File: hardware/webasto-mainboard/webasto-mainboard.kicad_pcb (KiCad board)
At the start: 4 copper layers, 86.8 x 76 mm, 100 parts, among them J1 Console FTDI, J2 DEBUG, J3 2-pole connector, Q1 DMG2301L, Q10 DMG2301L, Q11 SSM3J374R, Q12 2N7002, Q13 SUD50P04-08, Q14 SUD50P04-08, Q15 SUD50P04-08, Q16 SUD50P04-08, Q17 SUD50P04-08, Q18 2N7002, Q19 2N7002, Q2 2N7002, Q3 2N7002, Q4 2N7002, Q5 2N7002, Q6 SUD50P04-08, Q7 SUD50P04-08, Q8 SUD50P04-08, Q9 SUD50P04-08, U1 CY15E004J, U2 Pico, U3 LM4040DIM3-3.0, U4 MC33660BEFR2, U5 BD9G341EFJ, U6 LM7805_TO220, U7 INA219BxDCN

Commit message: Moved emerg. shutdown offboard
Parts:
- removed the D7 at (120.5, 103.9)
- removed the R16 at (136.1, 106.6)
- removed the R19 at (120.5, 103.9)
- J3: value 2-pole connector -> I2C; footprint Connector_PinHeader_2.54mm:PinHeader_1x02_P2.54mm_Horizontal -> Connector_PinHeader_2.54mm:PinHeader_1x04_P2.54mm_Vertical
- moved J3 8.16 mm to (108.5, 99.5), turned to 90 degrees
- renumbered D11 to D10, D12 to D11, D13 to D12, D8 to D7, D9 to D8, D10 to D9, R17 to R16, R18 to R17, R20 to R18, R21 to R19, R22 to R20, R23 to R21, R24 to R22, R25 to R23, R26 to R24, R27 to R25, R28 to R26, R29 to R27, R30 to R28, R31 to R29, R32 to R30, R33 to R31, R34 to R32, R35 to R33, R36 to R34
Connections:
- J3 pad 1: EmergencyStop -> SDA
- J3 pad 2: GND -> SCL
- U2 pad 21: ~{EmergencyStop3V} -> unconnected-(U2-Pad21)
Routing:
- net SDA: track 84.7 -> 140.1 mm, vias 2 -> 3
- net SCL: track 81.9 -> 130.7 mm, vias 3 -> 4
- net ~{EmergencyStop3V}: track 19.7 -> 0.00 mm, vias 1 -> 0
- net +3V3: track 50.6 -> 62.3 mm
- net ~{EmergencyStop}: track 6.21 -> 0.00 mm, vias 1 -> 0
- net Net-(Q2-Pad1): track 53.5 -> 50.3 mm
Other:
- board text added: "SDA SCL VCC GND"
- board text added: "v2.0 (c) 2023 Gavin Hurlbut"
- board text removed: "v1.0 (c) 2023 Gavin Hurlbut"

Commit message: Got rid of TINY diode (0402!?!?), remove USE_USB, put in PicoW
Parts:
- removed the J2 at (131.0, 98.2)
- removed JP1: SolderJumper_2_Open, Jumper:SolderJumper-2_P1.3mm_Open_TrianglePad1.0x1.5mm
- removed the R1 at (139.0, 104.6)
- C12: footprint Capacitor_SMD:C_0603_1608Metric_Pad1.08x0.95mm_HandSolder -> Capacitor_SMD:C_0805_2012Metric_Pad1.18x1.45mm_HandSolder
- D10: value ACDBQC0130L-HF -> BYS10-35; footprint Diode_SMD:D_SOD-923 -> Diode_SMD:D_SMA_Handsoldering; moved to F.Cu
- D7: value ACDBQC0130L-HF -> BYS10-35; footprint Diode_SMD:D_SOD-923 -> Diode_SMD:D_SMA_Handsoldering
- U2: value Pico -> PicoW; footprint MCU_RaspberryPi_and_Boards:RPi_Pico_SMD_TH -> RPi_Pico:RPi_PicoW_SMD_TH
- moved D10 5.44 mm to (104.5, 118.3), turned to 135 degrees
- moved D7 3.65 mm to (132.0, 71.4)
- moved D9 1.63 mm to (130.3, 67.8)
- moved C6 1.56 mm to (130.3, 64.6)
- renumbered J3 to J2, R2 to R1, R11 to R10, R12 to R11, R13 to R12, R14 to R13, R15 to R14, R16 to R15, R17 to R16, R18 to R17, R19 to R18, R20 to R19, R3 to R2, R21 to R20, R22 to R21, R23 to R22, R24 to R23, R25 to R24, R26 to R25, R27 to R26, R28 to R27, R29 to R28, R30 to R29, R4 to R3, R31 to R30, R32 to R31, R33 to R32, R34 to R33, R5 to R4, R6 to R5, R7 to R6, R8 to R7, R9 to R8, R10 to R9
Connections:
- U2 pad 22: UseUSB -> unconnected-(U2-Pad22)
- U2 pad 41: Net-(J2-Pad1) -> unconnected-(U2-Pad41)
- U2 pad 43: Net-(J2-Pad3) -> unconnected-(U2-Pad43)
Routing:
- net Net-(C7-Pad2): track 14.3 -> 21.0 mm
- net UseUSB: track 6.37 -> 0.00 mm
- net Net-(J2-Pad3): track 5.36 -> 0.00 mm
- net Net-(J2-Pad1): track 5.36 -> 0.00 mm
- net GND: track 63.1 -> 58.2 mm, vias 15 -> 16
- net Net-(D1-Pad2): track 38.8 -> 43.6 mm
- net +3V3: track 62.3 -> 59.1 mm, vias 10 -> 9
- net Net-(D7-Pad1): track 2.89 -> 4.59 mm
- net +12V: track 28.9 -> 27.8 mm, vias 13 -> 12

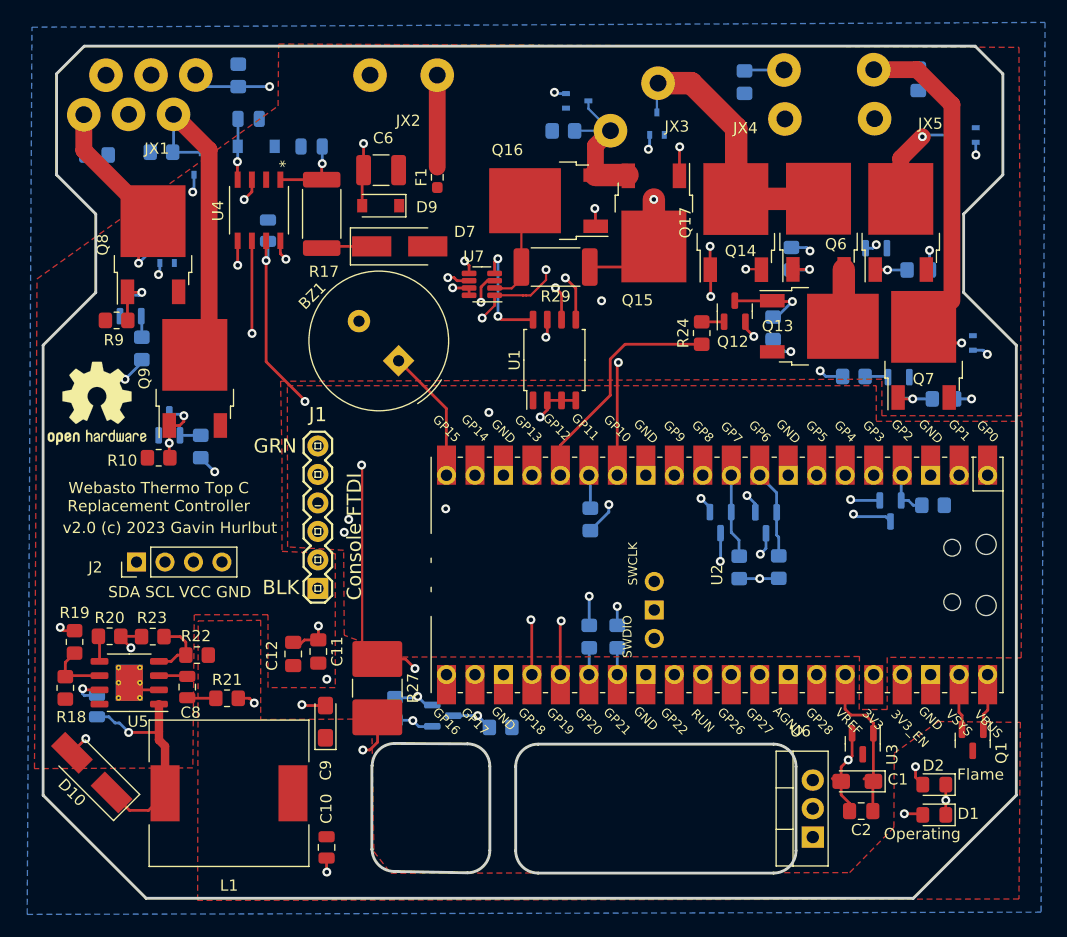
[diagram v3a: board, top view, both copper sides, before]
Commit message: Move VSYS to ADC2 to avoid the stupid WiFi setup
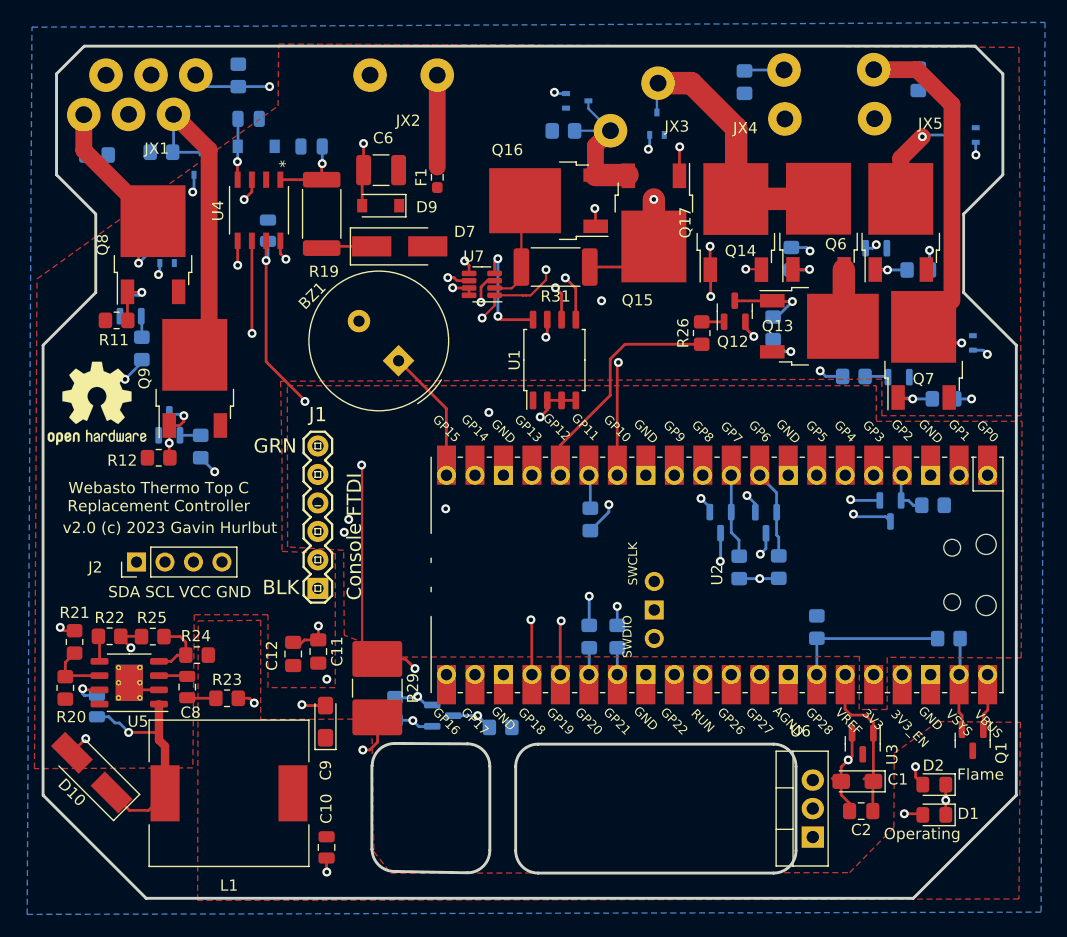
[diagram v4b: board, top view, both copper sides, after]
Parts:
- added R1: 200k, Resistor_SMD:R_0805_2012Metric_Pad1.20x1.40mm_HandSolder, B.Cu at (181.0, 106.4)
- added R2: 100k, Resistor_SMD:R_0805_2012Metric_Pad1.20x1.40mm_HandSolder, B.Cu at (169.2, 105.3)
- renumbered R8 to R10, R9 to R11, R10 to R12, R11 to R13, R12 to R14, R13 to R15, R14 to R16, R15 to R17, R16 to R18, R17 to R19, R18 to R20, R19 to R21, R20 to R22, R21 to R23, R22 to R24, R23 to R25, R24 to R26, R25 to R27, R26 to R28, R27 to R29, R1 to R3, R28 to R30, R29 to R31, R30 to R32, R31 to R33, R32 to R34, R33 to R35, R2 to R4, R3 to R5, R4 to R6, R5 to R7, R6 to R8, R7 to R9
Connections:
- net /ADC_VREF renamed ADC_VREF
- net /VSYS renamed VSYS
- U2 pad 34: unconnected-(U2-Pad34) -> VSYS_MON
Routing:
- net VSYS_MON: track 0.00 -> 14.0 mm
- net VSYS: track 5.00 -> 8.25 mm

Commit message: Move the LED to the mainboard
- due to how the driver doesn't share the SPI bus well, you currently can
  either use the TCP stack or the GPIOs.  Mixing will cause weird crashes.
- so I'm adding the LED onto the mainboard directly.
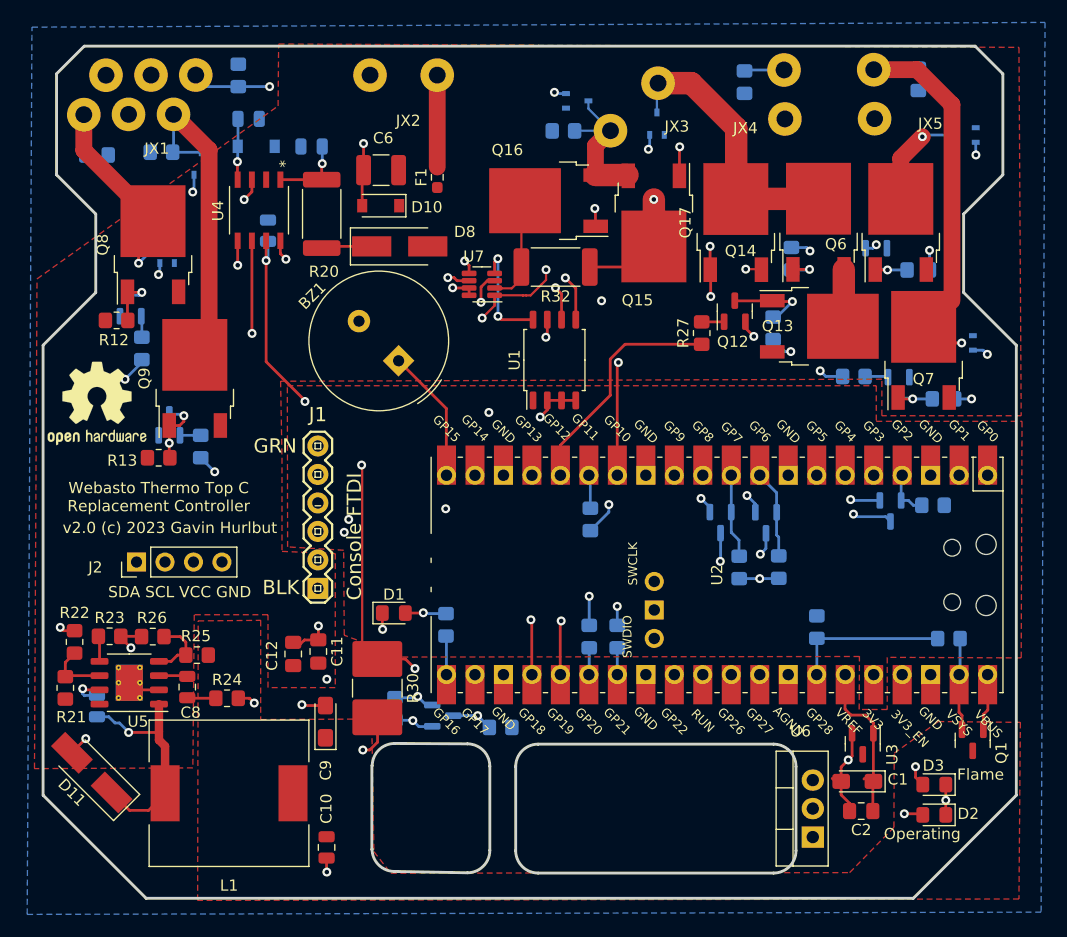
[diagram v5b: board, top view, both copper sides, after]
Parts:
- added D1: LED, LED_SMD:LED_0805_2012Metric_Pad1.15x1.40mm_HandSolder, F.Cu at (131.5, 104.1)
- added R3: 330R, Resistor_SMD:R_0805_2012Metric_Pad1.20x1.40mm_HandSolder, B.Cu at (136.1, 105.2)
- renumbered D9 to D10, D10 to D11, D11 to D12, D12 to D13, D1 to D2, D2 to D3, D3 to D4, D4 to D5, D5 to D6, D6 to D7, D7 to D8, D8 to D9, R9 to R10, R10 to R11, R11 to R12, R12 to R13, R13 to R14, R14 to R15, R15 to R16, R16 to R17, R17 to R18, R18 to R19, R19 to R20, R20 to R21, R21 to R22, R22 to R23, R23 to R24, R24 to R25, R25 to R26, R26 to R27, R27 to R28, R28 to R29, R29 to R30, R30 to R31, R31 to R32, R32 to R33, R33 to R34, R34 to R35, R35 to R36, R3 to R4, R4 to R5, R5 to R6, R6 to R7, R7 to R8, R8 to R9
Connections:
- U2 pad 21: unconnected-(U2-Pad21) -> Net-(U2-Pad21)
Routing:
- net Net-(D1-Pad2): track 0.00 -> 3.67 mm, vias 0 -> 1
- net Net-(U2-Pad21): track 0.00 -> 3.54 mm
- net GND: track 58.2 -> 59.6 mm, vias 16 -> 17

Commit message: Move start/run to sensor board, add CANBUS
- WiFi is not being very helpful, and I'm concerned it won't work well once
  installed in the bus...  CANBus wiring is easy.
- Removed both Start/Run and the Vehicle Fan Relay from X1 to make space for
  canbus
- moved LEDs onto an I2C gpio extender.
- will need to still plumb in CAN_EN support
- will also need to yank out the WiFi stuff that won't stay stable anyways
  and reroute the CBOR out the CANBus instead of WiFi
- Vehicle Fan control will need to move to a LINBus fan controller board
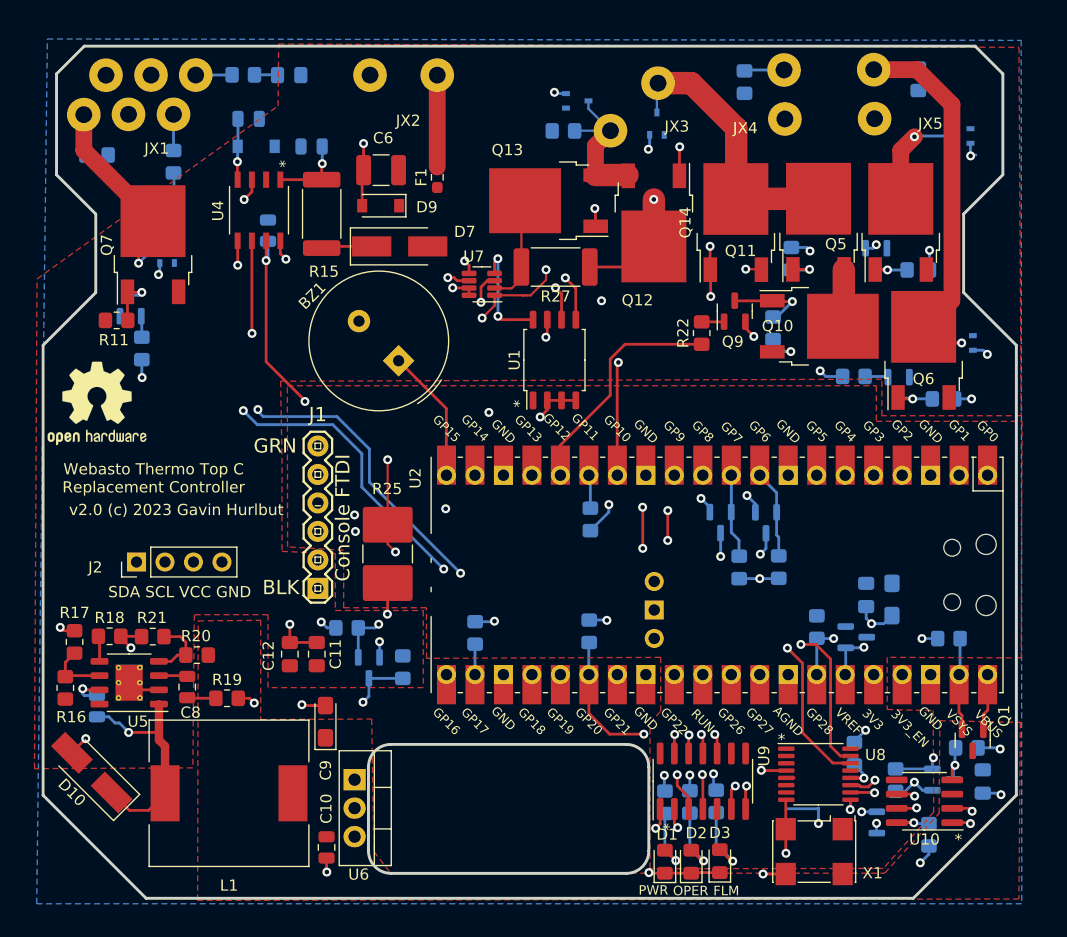
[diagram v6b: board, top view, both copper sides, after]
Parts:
- removed the D6 at (114.3, 64.0)
- removed the Q10 at (175.8, 95.0)
- removed the Q5 at (111.5, 87.3)
- removed the Q9 at (113.7, 83.2)
- removed the R13 at (110.5, 90.2)
- removed the R17 at (110.8, 63.0)
- removed the R18 at (117.6, 56.1)
- removed the R19 at (179.6, 94.5)
- removed the R9 at (114.2, 89.2)
- added C13: 1uF 6V3, Capacitor_SMD:C_0805_2012Metric_Pad1.18x1.45mm_HandSolder, B.Cu at (184.0, 119.1)
- added C14: 560pF, Capacitor_SMD:C_0805_2012Metric_Pad1.18x1.45mm_HandSolder, B.Cu at (122.1, 56.1)
- added C15: 560pF, Capacitor_SMD:C_0805_2012Metric_Pad1.18x1.45mm_HandSolder, B.Cu at (111.9, 67.9)
- added Q17: 2N7002, Package_TO_SOT_SMD:SOT-23, B.Cu at (180.4, 119.0)
- added Q18: 2N7002, Package_TO_SOT_SMD:SOT-23, B.Cu at (175.5, 122.8)
- added R32: 10k, Resistor_SMD:R_0805_2012Metric_Pad1.20x1.40mm_HandSolder, B.Cu at (138.7, 105.9)
- added R33: 10k, Resistor_SMD:R_0805_2012Metric_Pad1.20x1.40mm_HandSolder, B.Cu at (148.9, 105.7)
- added R34: 10k, Resistor_SMD:R_0805_2012Metric_Pad1.20x1.40mm_HandSolder, B.Cu at (176.2, 119.0)
- added R35: 10k, Resistor_SMD:R_0805_2012Metric_Pad1.20x1.40mm_HandSolder, B.Cu at (172.6, 116.7)
- added R36: 10k, Resistor_SMD:R_0805_2012Metric_Pad1.20x1.40mm_HandSolder, B.Cu at (182.6, 116.1)
- added R37: 10k, Resistor_SMD:R_0805_2012Metric_Pad1.20x1.40mm_HandSolder, B.Cu at (179.2, 123.9)
- added R38: 100, Resistor_SMD:R_0805_2012Metric_Pad1.20x1.40mm_HandSolder, B.Cu at (118.0, 56.1)
- added R39: 100, Resistor_SMD:R_0805_2012Metric_Pad1.20x1.40mm_HandSolder, B.Cu at (111.8, 63.9)
- added U10: MCP2557FD-xMF, Package_SO:SOIC-8_3.9x4.9mm_P1.27mm, F.Cu at (178.8, 120.9)
- added U8: TCA9534, Package_SO:TSSOP-16_4.4x5mm_P0.65mm, F.Cu at (169.3, 118.5)
- added U9: MCP2517FD, Package_SO:SOIC-14_3.9x8.7mm_P1.27mm, F.Cu at (159.0, 119.1)
- added X1: ASV-20.000MHZ-EJ-T, Oscillator:Oscillator_SMD_Abracon_ASV-4Pin_7.0x5.1mm, F.Cu at (169.0, 125.4)
- C1, C2, U3: moved to B.Cu
- R3: value 330R -> 1k
- moved U6 41.2 mm to (128.0, 119.0), turned to -90 degrees
- moved D1 32.8 mm to (155.7, 126.3), turned to 90 degrees
- moved R3 25.1 mm to (155.7, 121.0), turned to -90 degrees
- moved D2 22.1 mm to (158.0, 126.3), turned to 90 degrees
- moved D3 20.3 mm to (160.6, 126.2), turned to 90 degrees
- moved C2 19.3 mm to (173.6, 102.5), turned to 90 degrees
- moved R5 18.6 mm to (160.2, 120.9), turned to -90 degrees
- moved C1 16.5 mm to (175.9, 102.9), turned to 90 degrees
- moved R4 16.1 mm to (157.9, 121.0), turned to -90 degrees
- moved R25 12.0 mm to (130.9, 98.8)
- moved R23 10.2 mm to (132.3, 108.9), turned to 90 degrees
- moved U3 9.53 mm to (172.7, 106.2), turned to 0 degrees
- moved R30 8.39 mm to (127.3, 105.4), turned to 180 degrees
- moved Q8 7.85 mm to (129.2, 109.0), turned to -90 degrees
- moved D4 0.48 mm to (181.9, 61.5)
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- renumbered D11 to D10, D12 to D11, D13 to D12, D7 to D6, D8 to D7, D9 to D8, D10 to D9, Q13 to Q10, Q14 to Q11, Q15 to Q12, Q16 to Q13, Q17 to Q14, Q18 to Q15, Q19 to Q16, Q6 to Q5, Q7 to Q6, Q8 to Q7, Q11 to Q8, Q12 to Q9, R11 to R10, R12 to R11, R14 to R12, R15 to R13, R16 to R14, R20 to R15, R21 to R16, R22 to R17, R23 to R18, R24 to R19, R25 to R20, R26 to R21, R27 to R22, R28 to R23, R29 to R24, R30 to R25, R31 to R26, R32 to R27, R33 to R28, R34 to R29, R35 to R30, R36 to R31, R10 to R9
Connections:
- net ALERT renamed ALERT_PWM
- J1 pad 2: ConsoleCTS -> unconnected-(J1-Pad2)
- J1 pad 6: ConsoleRTS -> unconnected-(J1-Pad6)
- JX1 pad 1: StartRun -> CAN_HI
- JX1 pad 4: VehicleFanRelay -> CAN_LO
- R3 pad 1: Net-(U2-Pad21) -> PowerLED
- U2 pad 19: VehicleFanRelay3V -> unconnected-(U2-Pad19)
- U2 pad 21: Net-(U2-Pad21) -> MISO
- U2 pad 22: unconnected-(U2-Pad22) -> ~{SPI_SS}
- U2 pad 24: ConsoleCTS -> SCK
- U2 pad 25: ConsoleRTS -> MOSI
- U2 pad 26: FlameLED -> ~{CAN_INT}
- U2 pad 27: OperatingLED -> unconnected-(U2-Pad27)
- U2 pad 4: ~{StartRun3V} -> unconnected-(U2-Pad4)
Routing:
- net CAN_HI: track 0.00 -> 117.9 mm, vias 0 -> 3
- net CAN_LO: track 0.00 -> 114.3 mm, vias 0 -> 3
- net StartRun: track 97.3 -> 0.00 mm, vias 2 -> 0
- net ConsoleRTS: track 39.8 -> 0.00 mm, vias 1 -> 0
- net Net-(D3-Pad2): track 45.7 -> 6.51 mm, vias 2 -> 1
- net Net-(D2-Pad2): track 43.6 -> 6.28 mm, vias 2 -> 1
- net RXCAN_3V: track 0.00 -> 35.1 mm, vias 0 -> 2
- net SCL: track 130.7 -> 164.6 mm, vias 4 -> 7
- net Kelvin+: track 112.5 -> 79.0 mm
- net Net-(Q8-Pad3): track 45.7 -> 12.6 mm
- net TXCAN: track 0.00 -> 32.6 mm, vias 0 -> 2
- net SDA: track 140.1 -> 171.5 mm, vias 3 -> 6
- net VehicleFanRelay: track 29.3 -> 0.00 mm
- net MISO: track 0.00 -> 27.9 mm, vias 0 -> 1
- net ~{SPI_SS}: track 0.00 -> 26.8 mm, vias 0 -> 1
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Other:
- outline, holes or cut-outs redrawn
- board text added: "FLM"
- board text added: "OPER"
- board text added: "PWR"
- board text removed: "Flame"
- board text removed: "Operating"

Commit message: Rejigger the mainboard to use voltage regulator
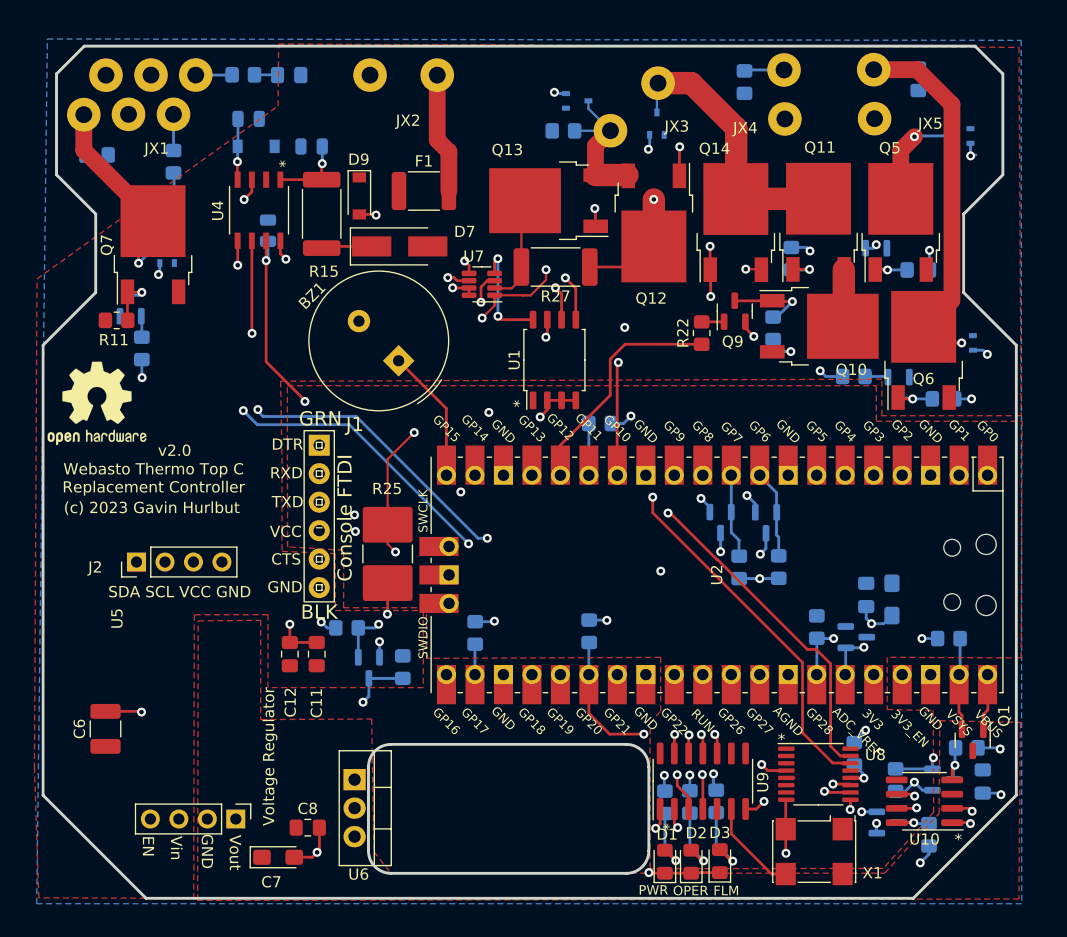
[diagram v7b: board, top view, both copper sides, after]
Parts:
- removed C10: 10uF, Capacitor_SMD:C_0805_2012Metric
- removed C9: 100uF Ta 6V, Capacitor_Tantalum_SMD:CP_EIA-3216-10_Kemet-I_Pad1.58x1.35mm_HandSolder
- removed D10: BYS10-35, Diode_SMD:D_SMA_Handsoldering
- removed L1: 33uH 5A 88mOhm, UltraLibrarian:PM4346.333NLT
- removed R16: 909k 1%, Resistor_SMD:R_0805_2012Metric_Pad1.20x1.40mm_HandSolder
- removed R17: 324k 1%, Resistor_SMD:R_0805_2012Metric_Pad1.20x1.40mm_HandSolder
- removed R18: 47k, Resistor_SMD:R_0805_2012Metric_Pad1.20x1.40mm_HandSolder
- removed R19: 6k2, Resistor_SMD:R_0805_2012Metric_Pad1.20x1.40mm_HandSolder
- removed R20: 3.0k, Resistor_SMD:R_0805_2012Metric_Pad1.20x1.40mm_HandSolder
- removed R21: 750R, Resistor_SMD:R_0805_2012Metric_Pad1.20x1.40mm_HandSolder
- C7: value 100nF -> 100uF Ta 6V; footprint Capacitor_SMD:C_0805_2012Metric -> Capacitor_Tantalum_SMD:CP_EIA-3216-10_Kemet-I_Pad1.58x1.35mm_HandSolder; moved to F.Cu
- C8: value 10nF -> 10uF; footprint Capacitor_SMD:C_0805_2012Metric -> Capacitor_SMD:C_0805_2012Metric_Pad1.18x1.45mm_HandSolder
- F1: footprint Resistor_SMD:R_0603_1608Metric_Pad0.98x0.95mm_HandSolder -> Resistor_SMD:R_1812_4532Metric_Pad1.30x3.40mm_HandSolder
- J1: footprint Beirdo:FTDI_BASIC -> Beirdo:FTDI-TARGET
- U2: footprint RPi_Pico:RPi_PicoW_SMD_TH -> MCU_RaspberryPi_and_Boards:RPi_Pico_SMD_TH
- U5: value BD9G341EFJ -> Voltage Regulator; footprint Package_SO:HTSOP-8-1EP_3.9x4.9mm_P1.27mm_EP2.4x3.2mm_ThermalVias -> Beirdo:Switching_Regulator_Module
- moved C6 55.6 mm to (105.8, 114.4), turned to 90 degrees
- moved C7 21.0 mm to (121.2, 125.9), turned to 0 degrees
- moved C8 16.5 mm to (123.8, 123.2), turned to 0 degrees
- moved U5 15.5 mm to (117.5, 122.4), turned to -90 degrees
- moved J1 12.8 mm to (124.8, 89.1), turned to -90 degrees
- moved R6 8.59 mm to (149.9, 87.2), turned to 0 degrees
- moved D9 2.09 mm to (128.4, 66.9), turned to -90 degrees
- moved F1 1.71 mm to (134.2, 66.5), turned to 0 degrees
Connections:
- net Net-(F1-Pad2) renamed +BATT
- C7 pad 1: Net-(C7-Pad1) -> +5V
- C7 pad 2: Net-(C7-Pad2) -> GND
- C8 pad 1: Net-(C8-Pad1) -> +5V
- C8 pad 2: Net-(C8-Pad2) -> GND
- J1 pad 1: GND -> unconnected-(J1-Pad1)
- J1 pad 2: unconnected-(J1-Pad2) -> ConsoleRX
- J1 pad 3: +3V3 -> ConsoleTX
- J1 pad 4: ConsoleTX -> +3V3
- J1 pad 5: ConsoleRX -> unconnected-(J1-Pad5)
- J1 pad 6: unconnected-(J1-Pad6) -> GND
- U5 pad 1: Net-(C7-Pad2) -> +5V
- U5 pad 3: Net-(C8-Pad1) -> +12V
- U5 pad 4: Net-(R20-Pad2) -> unconnected-(U5-Pad4)
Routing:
- net Net-(C7-Pad2): track 21.0 -> 0.00 mm, vias 1 -> 0
- net Net-(Q2-Pad1): track 50.3 -> 37.3 mm
- net GND: track 62.3 -> 51.3 mm, vias 18 -> 14
- net FlameLED: track 20.5 -> 14.2 mm
- net OperatingLED: track 22.4 -> 16.3 mm
- net Net-(R20-Pad2): track 5.94 -> 0.00 mm
- net Net-(R16-Pad2): track 5.85 -> 0.00 mm
- net Net-(U9-Pad6): track 13.1 -> 8.55 mm, vias 2 -> 0
- net +3V3: track 69.3 -> 65.0 mm, vias 14 -> 13
- net CAN_HI: track 117.9 -> 114.4 mm
- net Net-(C7-Pad1): track 3.35 -> 0.00 mm, vias 1 -> 0
- net Net-(C8-Pad2): track 2.57 -> 0.00 mm
- net +BATT: track 8.20 -> 10.8 mm
- net Net-(C8-Pad1): track 2.55 -> 0.00 mm
- net CAN_LO: track 114.3 -> 111.7 mm, vias 3 -> 4
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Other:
- board text added: "(c) 2023 Gavin Hurlbut"
- board text added: "v2.0"
- board text removed: "v2.0 (c) 2023 Gavin Hurlbut"
